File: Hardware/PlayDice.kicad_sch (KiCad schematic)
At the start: 31 parts, among them J1 Clock In, J2 Eurorack_10_pin_power, J3 Action In, J4 OLED, J5 Gate Out, J6 CV Out, Q1 MMBT3904, Q2 MMBT3904, U1 LM1117-5.0, U3 TL072

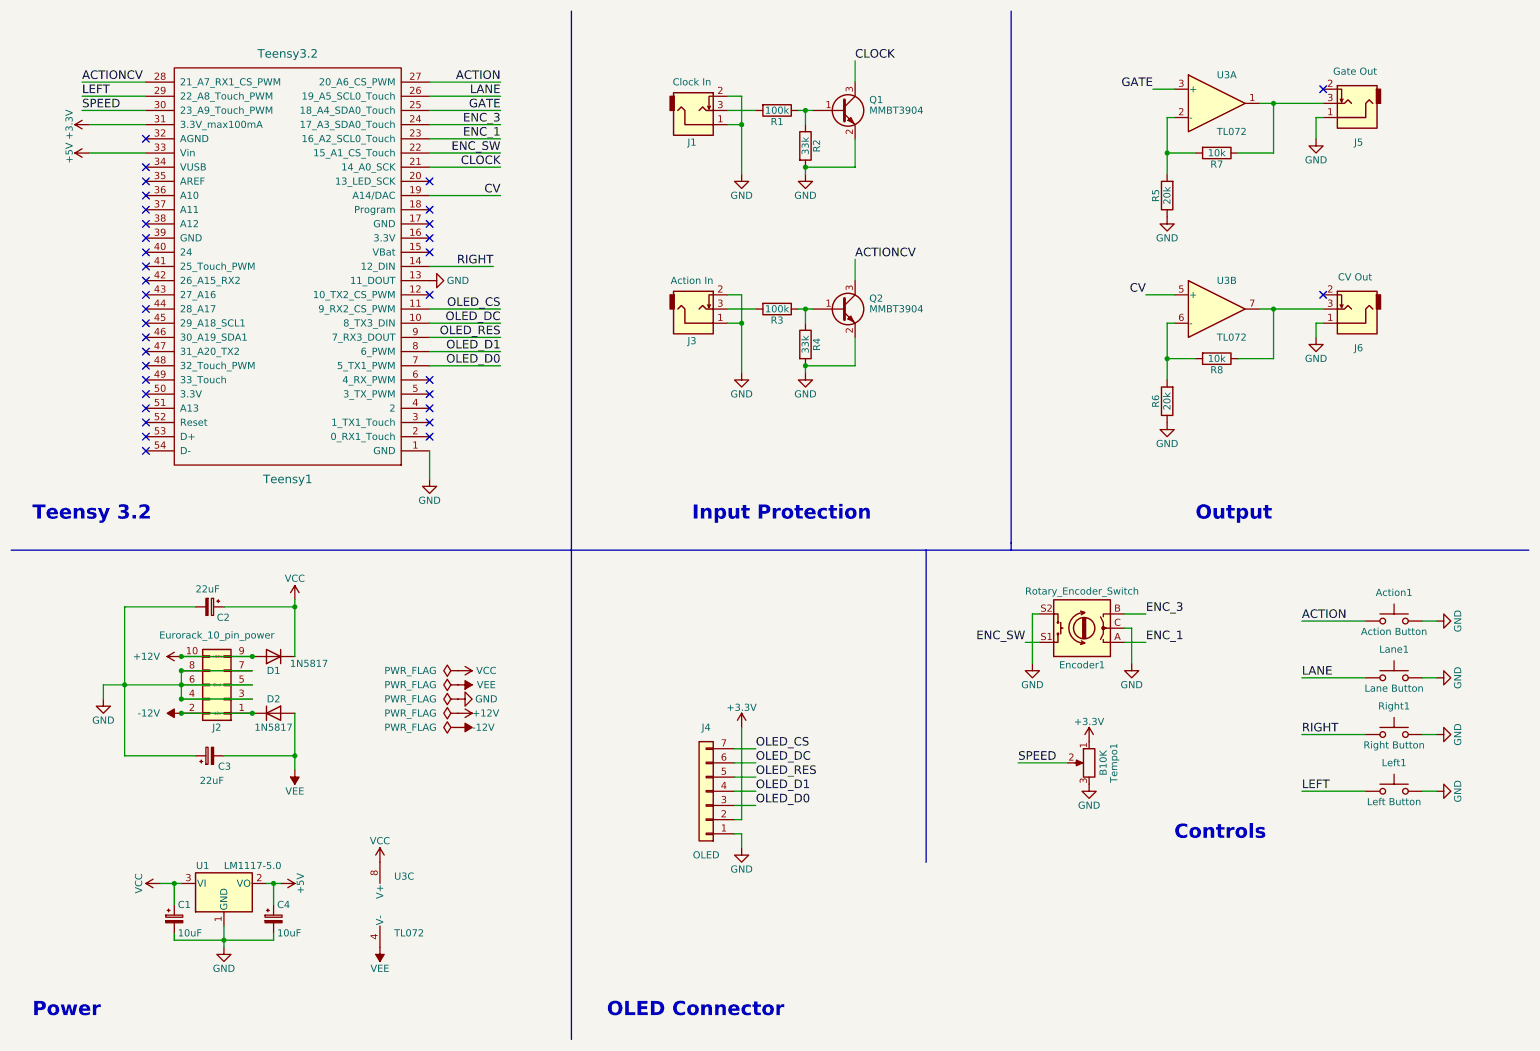
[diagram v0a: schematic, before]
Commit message: Updated to black and silver colour scheme; Transferred pcb and panel to Kicad 5.99
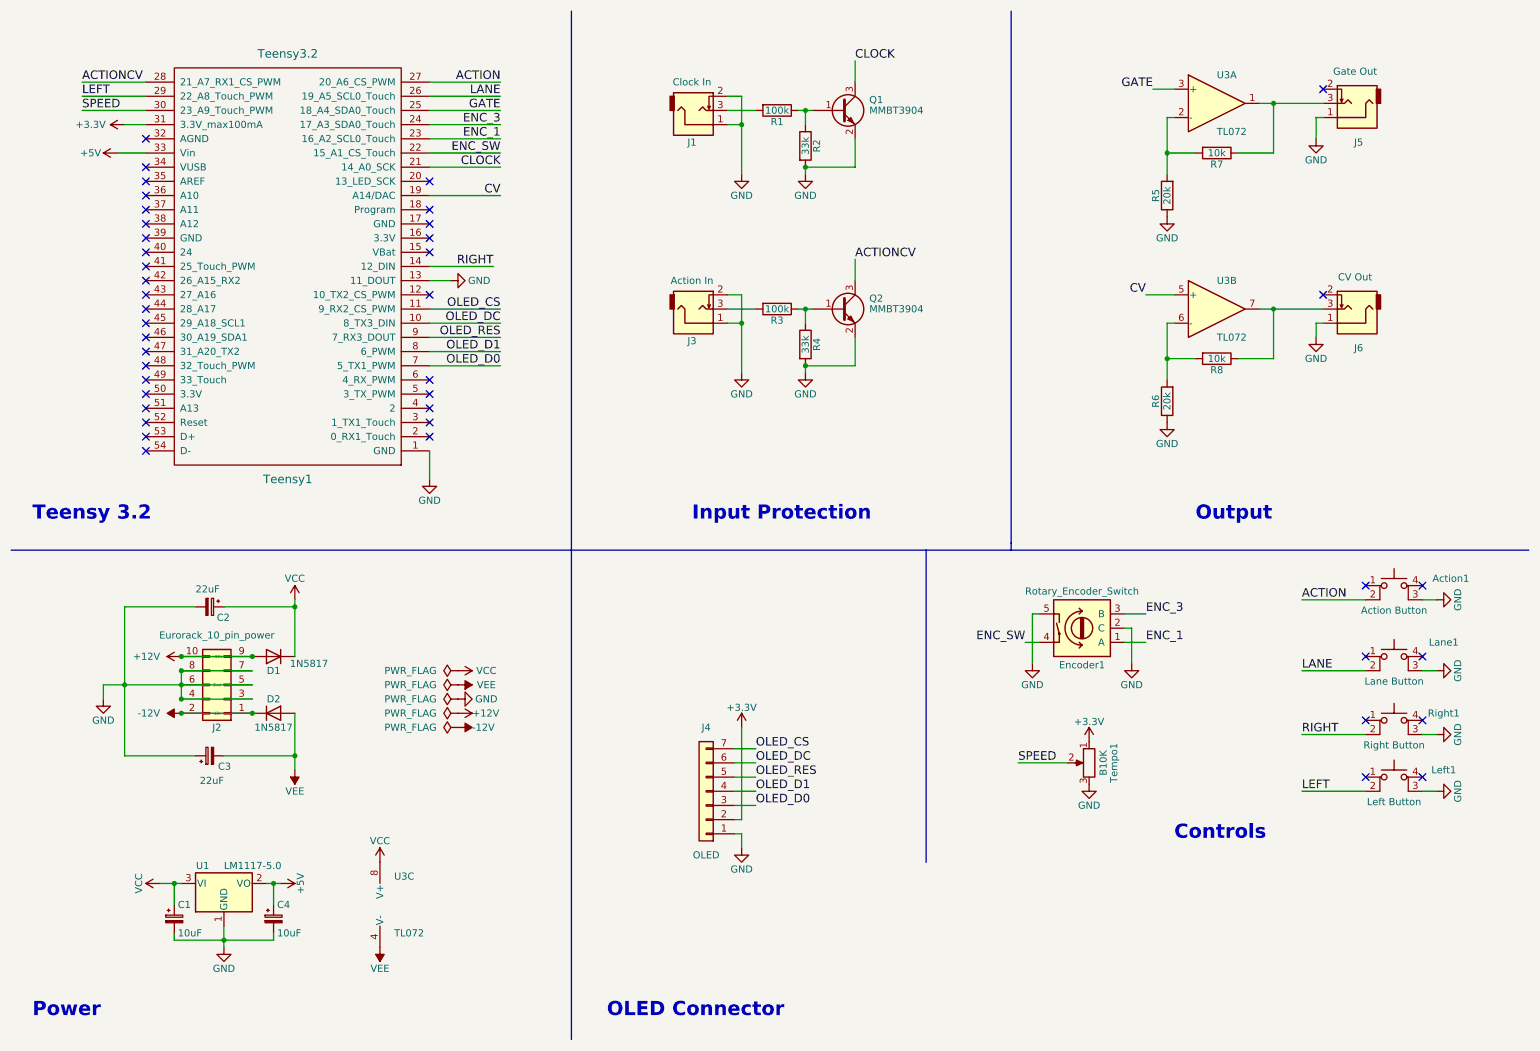
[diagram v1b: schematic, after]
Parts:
- Action1, Lane1, Left1, Right1: symbol Switch:SW_Push -> Switch:SW_MEC_5E
- C1, C4: footprint Capacitors_THT:CP_Radial_D5.0mm_P2.00mm -> Capacitor_SMD:C_0805_2012Metric_Pad1.18x1.45mm_HandSolder
- Encoder1: symbol Device:RotaryEncoder_Switch -> rotary_encoder:Rotary_Encoder_Switch
- J1, J3, J5, J6: footprint PlayDice:THONKICONN -> Custom_Footprints:THONKICONN_hole
- R1: footprint Resistors_SMD:R_0805_HandSoldering -> Resistor_SMD:R_0805_2012Metric_Pad1.20x1.40mm_HandSolder
- R2, R3, R4, R5, R6, R7, R8: footprint Resistors_THT:R_Axial_DIN0207_L6.3mm_D2.5mm_P10.16mm_Horizontal -> Resistor_SMD:R_0805_2012Metric_Pad1.20x1.40mm_HandSolder
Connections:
- net ACTION: now also Action1.2; no longer Action1.1
- net ENC_1: now also Encoder1.1 (A); no longer Encoder1.A
- net ENC_3: now also Encoder1.3 (B); no longer Encoder1.B
- net ENC_SW: now also Encoder1.4; no longer Encoder1.S1
- net GND: now also Action1.3 (K), Encoder1.2 (C), Encoder1.5, Lane1.3 (K), Left1.3 (K), Right1.3 (K); no longer Action1.2, Encoder1.C, Encoder1.S2, Lane1.2, Left1.2, Right1.2
- net LANE: now also Lane1.2; no longer Lane1.1
- net LEFT: now also Left1.2; no longer Left1.1
- net RIGHT: now also Right1.2; no longer Right1.1
- no-connect marks 35 -> 43
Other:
- company: (none) -> Mountjoy Modular
- title: (none) -> Play Dice
